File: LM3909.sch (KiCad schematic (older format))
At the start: 17 parts

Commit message: add values
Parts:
- R?: value R -> 12
- R? (x2): value R -> 410
- R?: value R -> 100
- R? (x2): value R -> 22K
- R?: value R -> 3.3K
- R?: value R -> 5.6K
- R?: value R -> 10K
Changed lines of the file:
@@
 P 2400 1700
 F 0 "R?" V 2480 1700 50  0000 C CNN
-F 1 "R" V 2400 1700 50  0000 C CNN
+F 1 "12" V 2400 1700 50  0000 C CNN
 F 2 "" V 2330 1700 50  0001 C CNN
 F 3 "" H 2400 1700 50  0001 C CNN
@@
 P 3600 1700
 F 0 "R?" V 3680 1700 50  0000 C CNN
-F 1 "R" V 3600 1700 50  0000 C CNN
+F 1 "410" V 3600 1700 50  0000 C CNN
 F 2 "" V 3530 1700 50  0001 C CNN
 F 3 "" H 3600 1700 50  0001 C CNN
@@
 P 3600 2150
 F 0 "R?" V 3680 2150 50  0000 C CNN
-F 1 "R" V 3600 2150 50  0000 C CNN
+F 1 "410" V 3600 2150 50  0000 C CNN
 F 2 "" V 3530 2150 50  0001 C CNN
 F 3 "" H 3600 2150 50  0001 C CNN
@@
 P 4800 3050
 F 0 "R?" V 4880 3050 50  0000 C CNN
-F 1 "R" V 4800 3050 50  0000 C CNN
+F 1 "100" V 4800 3050 50  0000 C CNN
 F 2 "" V 4730 3050 50  0001 C CNN
 F 3 "" H 4800 3050 50  0001 C CNN
@@
 P 3650 4150
 F 0 "R?" V 3730 4150 50  0000 C CNN
-F 1 "R" V 3650 4150 50  0000 C CNN
+F 1 "22K" V 3650 4150 50  0000 C CNN
 F 2 "" V 3580 4150 50  0001 C CNN
 F 3 "" H 3650 4150 50  0001 C CNN
@@
 P 2400 4200
 F 0 "R?" V 2480 4200 50  0000 C CNN
-F 1 "R" V 2400 4200 50  0000 C CNN
+F 1 "3.3K" V 2400 4200 50  0000 C CNN
 F 2 "" V 2330 4200 50  0001 C CNN
 F 3 "" H 2400 4200 50  0001 C CNN
@@
 P 2400 3500
 F 0 "R?" V 2480 3500 50  0000 C CNN
-F 1 "R" V 2400 3500 50  0000 C CNN
+F 1 "5.6K" V 2400 3500 50  0000 C CNN
 F 2 "" V 2330 3500 50  0001 C CNN
 F 3 "" H 2400 3500 50  0001 C CNN
@@
 P 4050 2200
 F 0 "R?" V 4130 2200 50  0000 C CNN
-F 1 "R" V 4050 2200 50  0000 C CNN
+F 1 "22K" V 4050 2200 50  0000 C CNN
 F 2 "" V 3980 2200 50  0001 C CNN
 F 3 "" H 4050 2200 50  0001 C CNN
@@
 P 4050 2650
 F 0 "R?" V 4130 2650 50  0000 C CNN
-F 1 "R" V 4050 2650 50  0000 C CNN
+F 1 "10K" V 4050 2650 50  0000 C CNN
 F 2 "" V 3980 2650 50  0001 C CNN
 F 3 "" H 4050 2650 50  0001 C CNN

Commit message: add reference designators
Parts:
- gave numbers to parts that had none: 16
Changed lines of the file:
@@
 $EndDescr
 $Comp
-L R R?
+L R R1
 U 1 1 5A1F12BF
 P 2400 1700
-F 0 "R?" V 2480 1700 50  0000 C CNN
+F 0 "R1" V 2480 1700 50  0000 C CNN
 F 1 "12" V 2400 1700 50  0000 C CNN
 F 2 "" V 2330 1700 50  0001 C CNN
@@
 $EndComp
 $Comp
-L R R?
+L R R4
 U 1 1 5A1F1353
 P 3600 1700
-F 0 "R?" V 3680 1700 50  0000 C CNN
+F 0 "R4" V 3680 1700 50  0000 C CNN
 F 1 "410" V 3600 1700 50  0000 C CNN
 F 2 "" V 3530 1700 50  0001 C CNN
@@
 $EndComp
 $Comp
-L R R?
+L R R5
 U 1 1 5A1F13B4
 P 3600 2150
-F 0 "R?" V 3680 2150 50  0000 C CNN
+F 0 "R5" V 3680 2150 50  0000 C CNN
 F 1 "410" V 3600 2150 50  0000 C CNN
 F 2 "" V 3530 2150 50  0001 C CNN
@@
 $EndComp
 $Comp
-L R R?
+L R R9
 U 1 1 5A1F13F7
 P 4800 3050
-F 0 "R?" V 4880 3050 50  0000 C CNN
+F 0 "R9" V 4880 3050 50  0000 C CNN
 F 1 "100" V 4800 3050 50  0000 C CNN
 F 2 "" V 4730 3050 50  0001 C CNN
@@
 $EndComp
 $Comp
-L R R?
+L R R8
 U 1 1 5A1F14BB
 P 3650 4150
-F 0 "R?" V 3730 4150 50  0000 C CNN
+F 0 "R8" V 3730 4150 50  0000 C CNN
 F 1 "22K" V 3650 4150 50  0000 C CNN
 F 2 "" V 3580 4150 50  0001 C CNN
@@
 $EndComp
 $Comp
-L R R?
+L R R3
 U 1 1 5A1F150A
 P 2400 4200
-F 0 "R?" V 2480 4200 50  0000 C CNN
+F 0 "R3" V 2480 4200 50  0000 C CNN
 F 1 "3.3K" V 2400 4200 50  0000 C CNN
 F 2 "" V 2330 4200 50  0001 C CNN
@@
 $EndComp
 $Comp
-L R R?
+L R R2
 U 1 1 5A1F1570
 P 2400 3500
-F 0 "R?" V 2480 3500 50  0000 C CNN
+F 0 "R2" V 2480 3500 50  0000 C CNN
 F 1 "5.6K" V 2400 3500 50  0000 C CNN
 F 2 "" V 2330 3500 50  0001 C CNN
@@
 $EndComp
 $Comp
-L C C?
+L C C1
 U 1 1 5A1F165A
 P 2800 2400
-F 0 "C?" H 2825 2500 50  0000 L CNN
+F 0 "C1" H 2825 2500 50  0000 L CNN
 F 1 "C" H 2825 2300 50  0000 L CNN
 F 2 "" H 2838 2250 50  0001 C CNN
@@
 $EndComp
 $Comp
-L 2N3904 Q?
+L 2N3904 Q4
 U 1 1 5A1F1805
 P 4350 1950
-F 0 "Q?" H 4550 2025 50  0000 L CNN
+F 0 "Q4" H 4550 2025 50  0000 L CNN
 F 1 "2N3904" H 4550 1950 50  0000 L CNN
 F 2 "TO_SOT_Packages_THT:TO-92_Molded_Narrow" H 4550 1875 50  0001 L CIN
@@
 $EndComp
 $Comp
-L 2N3904 Q?
+L 2N3904 Q1
 U 1 1 5A1F18F8
 P 4700 2450
-F 0 "Q?" H 4900 2525 50  0000 L CNN
+F 0 "Q1" H 4900 2525 50  0000 L CNN
 F 1 "2N3904" H 4900 2450 50  0000 L CNN
 F 2 "TO_SOT_Packages_THT:TO-92_Molded_Narrow" H 4900 2375 50  0001 L CIN
@@
 $EndComp
 $Comp
-L 2N3904 Q?
+L 2N3904 Q3
 U 1 1 5A1F1969
 P 3100 3750
-F 0 "Q?" H 3300 3825 50  0000 L CNN
+F 0 "Q3" H 3300 3825 50  0000 L CNN
 F 1 "2N3904" H 3300 3750 50  0000 L CNN
 F 2 "TO_SOT_Packages_THT:TO-92_Molded_Narrow" H 3300 3675 50  0001 L CIN
@@
 $EndComp
 $Comp
-L 2N3906 Q?
+L 2N3906 Q2B
 U 1 1 5A1F19DC
 P 6250 1850
-F 0 "Q?" H 6450 1925 50  0000 L CNN
+F 0 "Q2B" H 6450 1925 50  0000 L CNN
 F 1 "2N3906" H 6450 1850 50  0000 L CNN
 F 2 "TO_SOT_Packages_THT:TO-92_Molded_Narrow" H 6450 1775 50  0001 L CIN
@@
 $EndComp
 $Comp
-L 2N3906 Q?
+L 2N3906 Q2A
 U 1 1 5A1F1AC4
 P 5300 1850
-F 0 "Q?" H 5500 1925 50  0000 L CNN
+F 0 "Q2A" H 5500 1925 50  0000 L CNN
 F 1 "2N3906" H 5500 1850 50  0000 L CNN
 F 2 "TO_SOT_Packages_THT:TO-92_Molded_Narrow" H 5500 1775 50  0001 L CIN
@@
 $EndComp
 $Comp
-L R R?
+L R R6
 U 1 1 5A1F2593
 P 4050 2200
-F 0 "R?" V 4130 2200 50  0000 C CNN
+F 0 "R6" V 4130 2200 50  0000 C CNN
 F 1 "22K" V 4050 2200 50  0000 C CNN
 F 2 "" V 3980 2200 50  0001 C CNN
@@
 $EndComp
 $Comp
-L R R?
+L R R7
 U 1 1 5A1F25EB
 P 4050 2650
-F 0 "R?" V 4130 2650 50  0000 C CNN
+F 0 "R7" V 4130 2650 50  0000 C CNN
 F 1 "10K" V 4050 2650 50  0000 C CNN
 F 2 "" V 3980 2650 50  0001 C CNN
@@
 $EndComp
 $Comp
-L LED D?
+L LED D1
 U 1 1 5A1F2888
 P 2400 2150
-F 0 "D?" H 2400 2250 50  0000 C CNN
+F 0 "D1" H 2400 2250 50  0000 C CNN
 F 1 "LED" H 2400 2050 50  0000 C CNN
 F 2 "" H 2400 2150 50  0001 C CNN

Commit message: add 0805 footprints to many components
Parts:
- C1: footprint (none) -> Capacitors_SMD:C_0805
- D1: footprint (none) -> LEDs:LED_0805
- R1, R2, R3, R4, R5, R6, R7, R8, R9: footprint (none) -> Resistors_SMD:R_0805
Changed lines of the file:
@@
 LIBS:contrib
 LIBS:valves
+LIBS:LM3909-cache
 EELAYER 25 0
 EELAYER END
@@
 F 0 "R1" V 2480 1700 50  0000 C CNN
 F 1 "12" V 2400 1700 50  0000 C CNN
-F 2 "" V 2330 1700 50  0001 C CNN
+F 2 "Resistors_SMD:R_0805" V 2330 1700 50  0001 C CNN
 F 3 "" H 2400 1700 50  0001 C CNN
 	1    2400 1700
@@
 F 0 "R4" V 3680 1700 50  0000 C CNN
 F 1 "410" V 3600 1700 50  0000 C CNN
-F 2 "" V 3530 1700 50  0001 C CNN
+F 2 "Resistors_SMD:R_0805" V 3530 1700 50  0001 C CNN
 F 3 "" H 3600 1700 50  0001 C CNN
 	1    3600 1700
@@
 F 0 "R5" V 3680 2150 50  0000 C CNN
 F 1 "410" V 3600 2150 50  0000 C CNN
-F 2 "" V 3530 2150 50  0001 C CNN
+F 2 "Resistors_SMD:R_0805" V 3530 2150 50  0001 C CNN
 F 3 "" H 3600 2150 50  0001 C CNN
 	1    3600 2150
@@
 F 0 "R9" V 4880 3050 50  0000 C CNN
 F 1 "100" V 4800 3050 50  0000 C CNN
-F 2 "" V 4730 3050 50  0001 C CNN
+F 2 "Resistors_SMD:R_0805" V 4730 3050 50  0001 C CNN
 F 3 "" H 4800 3050 50  0001 C CNN
 	1    4800 3050
@@
 F 0 "R8" V 3730 4150 50  0000 C CNN
 F 1 "22K" V 3650 4150 50  0000 C CNN
-F 2 "" V 3580 4150 50  0001 C CNN
+F 2 "Resistors_SMD:R_0805" V 3580 4150 50  0001 C CNN
 F 3 "" H 3650 4150 50  0001 C CNN
 	1    3650 4150
@@
 F 0 "R3" V 2480 4200 50  0000 C CNN
 F 1 "3.3K" V 2400 4200 50  0000 C CNN
-F 2 "" V 2330 4200 50  0001 C CNN
+F 2 "Resistors_SMD:R_0805" V 2330 4200 50  0001 C CNN
 F 3 "" H 2400 4200 50  0001 C CNN
 	1    2400 4200
@@
 F 0 "R2" V 2480 3500 50  0000 C CNN
 F 1 "5.6K" V 2400 3500 50  0000 C CNN
-F 2 "" V 2330 3500 50  0001 C CNN
+F 2 "Resistors_SMD:R_0805" V 2330 3500 50  0001 C CNN
 F 3 "" H 2400 3500 50  0001 C CNN
 	1    2400 3500
@@
 F 0 "C1" H 2825 2500 50  0000 L CNN
 F 1 "C" H 2825 2300 50  0000 L CNN
-F 2 "" H 2838 2250 50  0001 C CNN
+F 2 "Capacitors_SMD:C_0805" H 2838 2250 50  0001 C CNN
 F 3 "" H 2800 2400 50  0001 C CNN
 	1    2800 2400
@@
 F 0 "R6" V 4130 2200 50  0000 C CNN
 F 1 "22K" V 4050 2200 50  0000 C CNN
-F 2 "" V 3980 2200 50  0001 C CNN
+F 2 "Resistors_SMD:R_0805" V 3980 2200 50  0001 C CNN
 F 3 "" H 4050 2200 50  0001 C CNN
 	1    4050 2200
@@
 F 0 "R7" V 4130 2650 50  0000 C CNN
 F 1 "10K" V 4050 2650 50  0000 C CNN
-F 2 "" V 3980 2650 50  0001 C CNN
+F 2 "Resistors_SMD:R_0805" V 3980 2650 50  0001 C CNN
 F 3 "" H 4050 2650 50  0001 C CNN
 	1    4050 2650
@@
 F 0 "D1" H 2400 2250 50  0000 C CNN
 F 1 "LED" H 2400 2050 50  0000 C CNN
-F 2 "" H 2400 2150 50  0001 C CNN
+F 2 "LEDs:LED_0805" H 2400 2150 50  0001 C CNN
 F 3 "" H 2400 2150 50  0001 C CNN
 	1    2400 2150

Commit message: generate netlist
and automatically rename Q2x to Q2x1
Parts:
- gave numbers to parts that had none: 1
- renumbered Q2A to Q2A1, Q2B to Q2B1
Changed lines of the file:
@@
 $EndComp
 $Comp
-L 2N3906 Q2B
+L 2N3906 Q2B1
 U 1 1 5A1F19DC
 P 6250 1850
-F 0 "Q2B" H 6450 1925 50  0000 L CNN
+F 0 "Q2B1" H 6450 1925 50  0000 L CNN
 F 1 "2N3906" H 6450 1850 50  0000 L CNN
 F 2 "TO_SOT_Packages_THT:TO-92_Molded_Narrow" H 6450 1775 50  0001 L CIN
@@
 $EndComp
 $Comp
-L 2N3906 Q2A
+L 2N3906 Q2A1
 U 1 1 5A1F1AC4
 P 5300 1850
-F 0 "Q2A" H 5500 1925 50  0000 L CNN
+F 0 "Q2A1" H 5500 1925 50  0000 L CNN
 F 1 "2N3906" H 5500 1850 50  0000 L CNN
 F 2 "TO_SOT_Packages_THT:TO-92_Molded_Narrow" H 5500 1775 50  0001 L CIN
@@
 	6350 3750 6350 2050
 $Comp
-L Battery_Cell BT?
+L Battery_Cell BT1
 U 1 1 5A1F4857
 P 6900 3250
-F 0 "BT?" H 7000 3350 50  0000 L CNN
+F 0 "BT1" H 7000 3350 50  0000 L CNN
 F 1 "Battery_Cell" H 7000 3250 50  0000 L CNN
 F 2 "" V 6900 3310 50  0001 C CNN

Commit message: replace through hole transistors with smd parts
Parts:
- removed Q1, Q3, Q4: 2N3904, TO_SOT_Packages_THT:TO-92_Molded_Narrow, symbol 2N3904
- removed Q2A1, Q2B1: 2N3906, TO_SOT_Packages_THT:TO-92_Molded_Narrow, symbol 2N3906
- added Q1, Q3, Q4: BC847, TO_SOT_Packages_SMD:SOT-23, symbol BC847
- added Q2A1, Q2B1: BC807, TO_SOT_Packages_SMD:SOT-23, symbol BC807
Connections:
- net at BT1.1 (+), R1.1, R4.1: now also Q2A1.2 (E), Q2B1.2 (E), Q4.3 (C)
- net at R4.2, R5.1, R6.1: now also Q4.1 (B)
- net at C1.1, R5.2: now also Q3.3 (C)
- net at R9.1: now also Q1.2 (E)
- net at R7.2, R8.1: now also Q4.2 (E)
- net at BT1.2 (-), R3.2, R8.2: now also Q3.2 (E)
- net at R6.2, R7.1: now also Q1.1 (B)
- new net: Q1.3 (C), Q2A1.1 (B), Q2A1.3 (C), Q2B1.1 (B)
- new net: Q2B1.3 (C), Q3.1 (B)
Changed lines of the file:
@@
-$EndComp
-$Comp
-L 2N3904 Q4
-U 1 1 5A1F1805
-P 4350 1950
-F 0 "Q4" H 4550 2025 50  0000 L CNN
-F 1 "2N3904" H 4550 1950 50  0000 L CNN
-F 2 "TO_SOT_Packages_THT:TO-92_Molded_Narrow" H 4550 1875 50  0001 L CIN
-F 3 "" H 4350 1950 50  0001 L CNN
-	1    4350 1950
-	1    0    0    -1
-$EndComp
-$Comp
-L 2N3904 Q1
-U 1 1 5A1F18F8
-P 4700 2450
-F 0 "Q1" H 4900 2525 50  0000 L CNN
-F 1 "2N3904" H 4900 2450 50  0000 L CNN
-F 2 "TO_SOT_Packages_THT:TO-92_Molded_Narrow" H 4900 2375 50  0001 L CIN
-F 3 "" H 4700 2450 50  0001 L CNN
-	1    4700 2450
-	1    0    0    -1
-$EndComp
-$Comp
-L 2N3904 Q3
-U 1 1 5A1F1969
-P 3100 3750
-F 0 "Q3" H 3300 3825 50  0000 L CNN
-F 1 "2N3904" H 3300 3750 50  0000 L CNN
-F 2 "TO_SOT_Packages_THT:TO-92_Molded_Narrow" H 3300 3675 50  0001 L CIN
-F 3 "" H 3100 3750 50  0001 L CNN
-	1    3100 3750
-	-1   0    0    -1
-$EndComp
-$Comp
-L 2N3906 Q2B1
-U 1 1 5A1F19DC
-P 6250 1850
-F 0 "Q2B1" H 6450 1925 50  0000 L CNN
-F 1 "2N3906" H 6450 1850 50  0000 L CNN
-F 2 "TO_SOT_Packages_THT:TO-92_Molded_Narrow" H 6450 1775 50  0001 L CIN
-F 3 "" H 6250 1850 50  0001 L CNN
-	1    6250 1850
-	1    0    0    1
-$EndComp
-$Comp
-L 2N3906 Q2A1
-U 1 1 5A1F1AC4
-P 5300 1850
-F 0 "Q2A1" H 5500 1925 50  0000 L CNN
-F 1 "2N3906" H 5500 1850 50  0000 L CNN
-F 2 "TO_SOT_Packages_THT:TO-92_Molded_Narrow" H 5500 1775 50  0001 L CIN
-F 3 "" H 5300 1850 50  0001 L CNN
-	1    5300 1850
-	-1   0    0    1
 $EndComp
 $Comp
@@
 	6900 4450 6900 3350
 Connection ~ 3650 4450
+$Comp
+L BC847 Q4
+U 1 1 5A204D01
+P 4350 1950
+F 0 "Q4" H 4550 2025 50  0000 L CNN
+F 1 "BC847" H 4550 1950 50  0000 L CNN
+F 2 "TO_SOT_Packages_SMD:SOT-23" H 4550 1875 50  0001 L CIN
+F 3 "" H 4350 1950 50  0001 L CNN
+	1    4350 1950
+	1    0    0    -1
+$EndComp
+$Comp
+L BC847 Q1
+U 1 1 5A2054C7
+P 4700 2450
+F 0 "Q1" H 4900 2525 50  0000 L CNN
+F 1 "BC847" H 4900 2450 50  0000 L CNN
+F 2 "TO_SOT_Packages_SMD:SOT-23" H 4900 2375 50  0001 L CIN
+F 3 "" H 4700 2450 50  0001 L CNN
+	1    4700 2450
+	1    0    0    -1
+$EndComp
+$Comp
+L BC847 Q3
+U 1 1 5A205527
+P 3100 3750
+F 0 "Q3" H 3300 3825 50  0000 L CNN
+F 1 "BC847" H 3300 3750 50  0000 L CNN
+F 2 "TO_SOT_Packages_SMD:SOT-23" H 3300 3675 50  0001 L CIN
+F 3 "" H 3100 3750 50  0001 L CNN
+	1    3100 3750
+	-1   0    0    -1
+$EndComp
+$Comp
+L BC807 Q2B1
+U 1 1 5A205CDD
+P 6250 1850
+F 0 "Q2B1" H 6450 1925 50  0000 L CNN
+F 1 "BC807" H 6450 1850 50  0000 L CNN
+F 2 "TO_SOT_Packages_SMD:SOT-23" H 6450 1775 50  0001 L CIN
+F 3 "" H 6250 1850 50  0001 L CNN
+	1    6250 1850
+	1    0    0    1
+$EndComp
+$Comp
+L BC807 Q2A1
+U 1 1 5A205D5E
+P 5300 1850
+F 0 "Q2A1" H 5500 1925 50  0000 L CNN
+F 1 "BC807" H 5500 1850 50  0000 L CNN
+F 2 "TO_SOT_Packages_SMD:SOT-23" H 5500 1775 50  0001 L CIN
+F 3 "" H 5300 1850 50  0001 L CNN
+	1    5300 1850
+	-1   0    0    1
+$EndComp
 $EndSCHEMATC

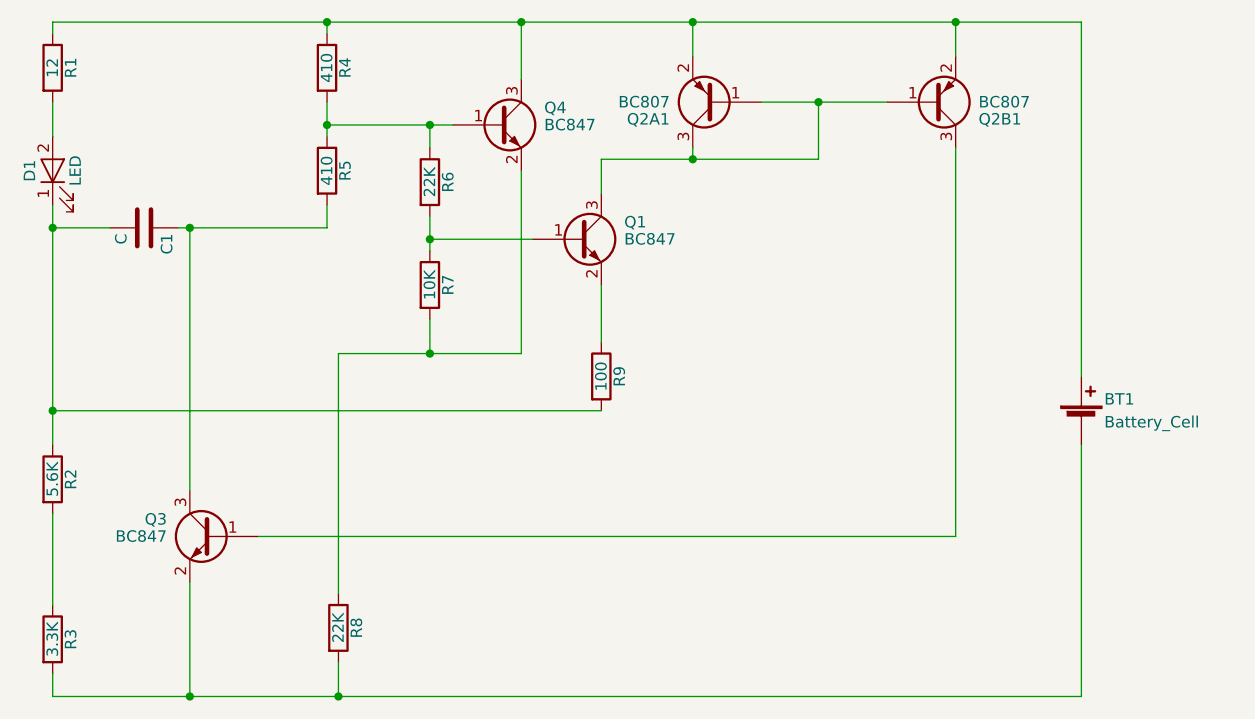
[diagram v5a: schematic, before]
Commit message: add another R that can be used intead of transistor current mirror
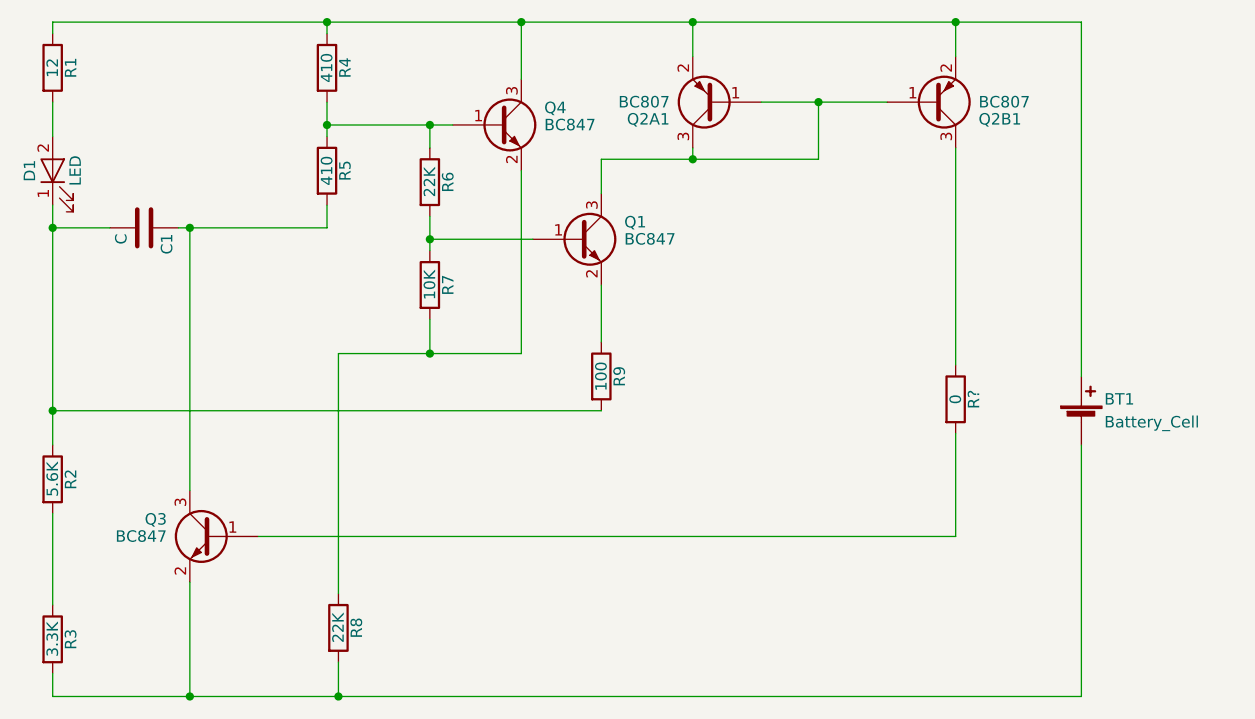
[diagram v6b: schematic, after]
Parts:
- added R?: 0, Resistors_SMD:R_0805, symbol R
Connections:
- net at Q3.1 (B): now also R?.2; no longer Q2B1.3 (C)
- new net: Q2B1.3 (C), R?.1
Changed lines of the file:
@@
 Wire Wire Line
 	3300 3750 6350 3750
-Wire Wire Line
-	6350 3750 6350 2050
 $Comp
 L Battery_Cell BT1
@@
 	-1   0    0    1
 $EndComp
+$Comp
+L R R?
+U 1 1 5A206553
+P 6350 3150
+F 0 "R?" V 6430 3150 50  0000 C CNN
+F 1 "0" V 6350 3150 50  0000 C CNN
+F 2 "Resistors_SMD:R_0805" V 6280 3150 50  0001 C CNN
+F 3 "" H 6350 3150 50  0001 C CNN
+	1    6350 3150
+	1    0    0    -1
+$EndComp
+Wire Wire Line
+	6350 2050 6350 3000
+Wire Wire Line
+	6350 3750 6350 3300
 $EndSCHEMATC

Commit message: route some more
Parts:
- gave numbers to parts that had none: 1
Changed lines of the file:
@@
 $EndComp
 $Comp
-L R R?
+L R R10
 U 1 1 5A206553
 P 6350 3150
-F 0 "R?" V 6430 3150 50  0000 C CNN
+F 0 "R10" V 6430 3150 50  0000 C CNN
 F 1 "0" V 6350 3150 50  0000 C CNN
 F 2 "Resistors_SMD:R_0805" V 6280 3150 50  0001 C CNN

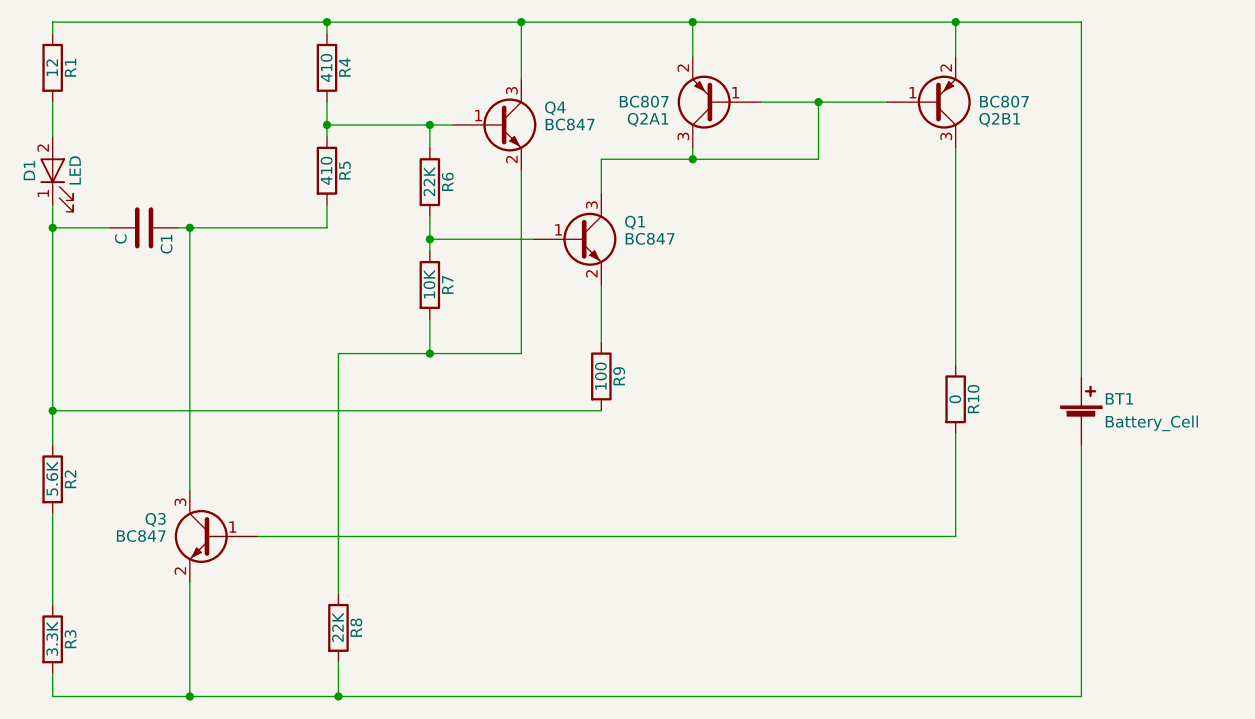
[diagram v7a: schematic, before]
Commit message: condense schematic
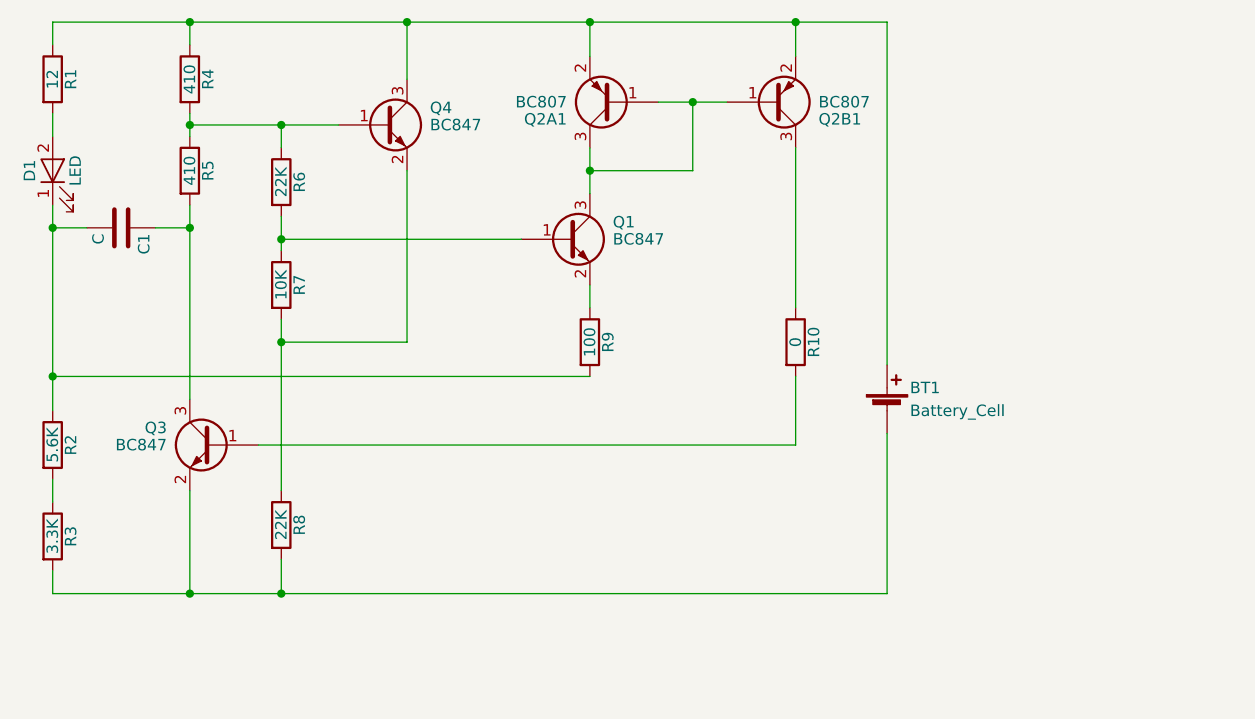
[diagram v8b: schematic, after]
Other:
- moved on the sheet: BT1, C1, Q1, Q2A1, Q2B1, Q3, Q4, R1, R10, R2, R3, R4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
